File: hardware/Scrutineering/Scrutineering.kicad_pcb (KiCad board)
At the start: 2 copper layers, 52.8 x 51.7 mm, 22 parts, among them J1 Conn_02x04, J10 Conn_01x01, J11 Conn_01x02, J12 Conn_01x02, J2 Conn_02x04, J3 Conn_01x03, J4 Conn_01x03, J5 Conn_01x01, J6 Conn_01x01, J7 Conn_01x01, J8 Conn_01x01, J9 Conn_01x01

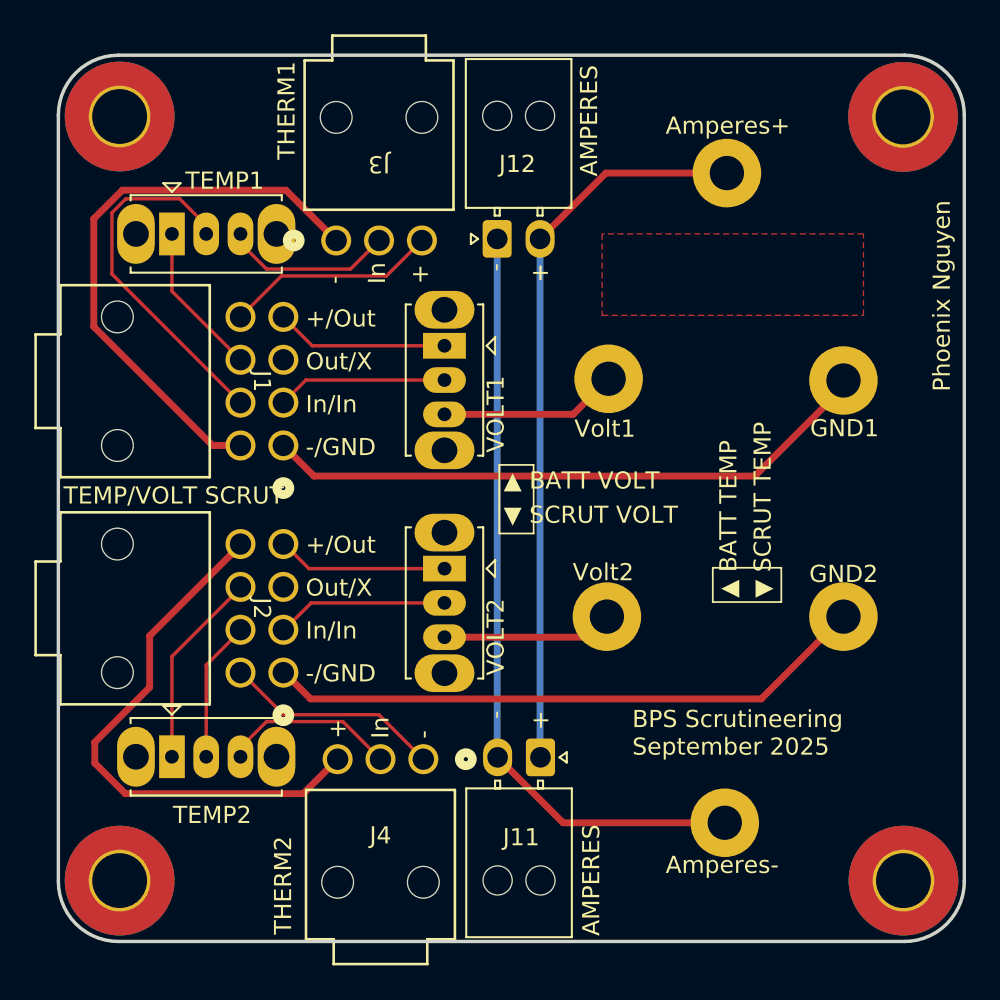
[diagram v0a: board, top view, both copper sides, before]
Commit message: changed to vertical connectors
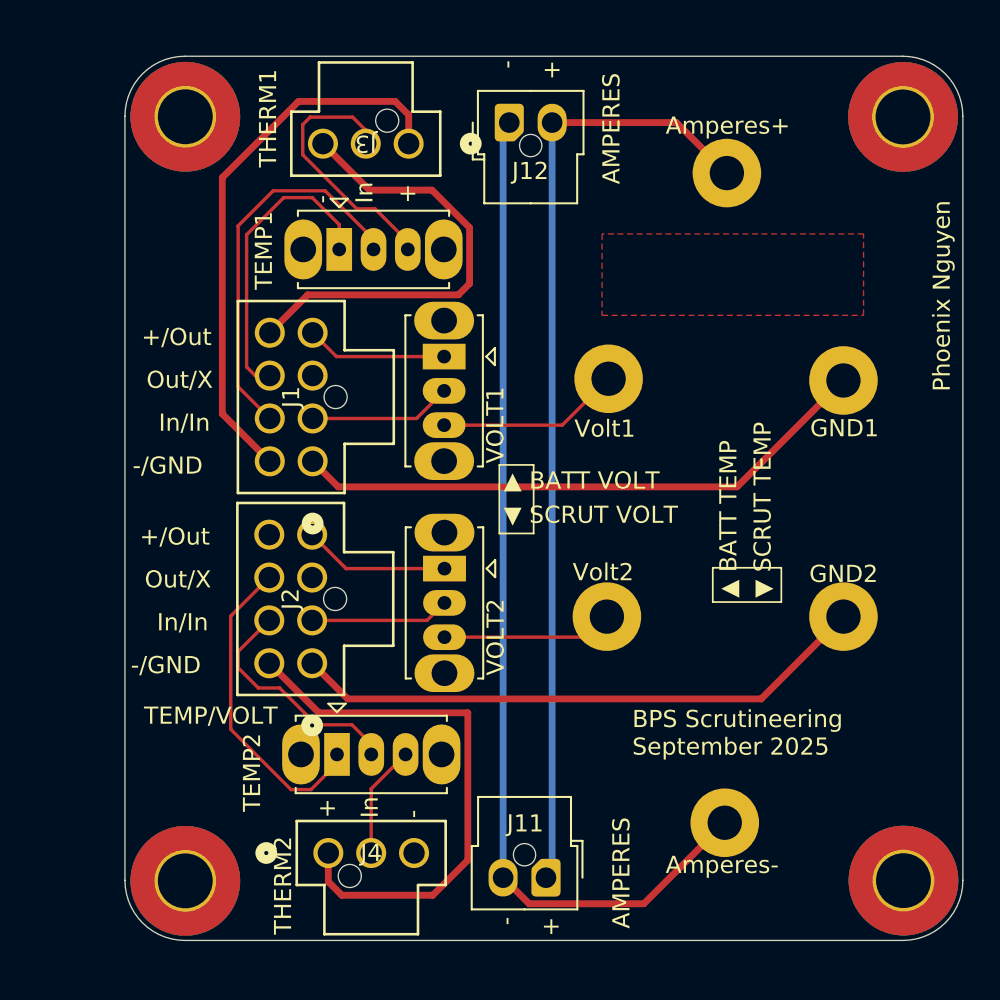
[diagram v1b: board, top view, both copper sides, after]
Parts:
- J1, J2: footprint Scrutineering:nanofit_02x04 -> Scrutineering:CONN_SD-105310-100_08_MOL
- J11, J12: footprint UTSVT_Connectors:105313-2102 -> UTSVT_Connectors:Molex_Nano-Fit_105309-xx02_1x02_P2.50mm_Vertical
- J3, J4: footprint VoltTemp:1053131103 -> Scrutineering:CONN_SD-105309-100_03_MOL
- moved TEMP1 9.80 mm to (103.8, 63.8)
- moved TEMP2 9.63 mm to (103.6, 93.2)
- moved J4 7.79 mm to (103.1, 99.0)
- moved J3 7.05 mm to (107.8, 57.6)
- moved J11 7.03 mm to (115.8, 100.4)
- moved J12 6.82 mm to (113.7, 56.4)
- moved MH3 3.83 mm to (94.8, 56.0)
- moved MH4 3.83 mm to (94.8, 100.6)
- moved J1 1.94 mm to (102.2, 76.1), turned to 90 degrees
- moved J2 1.77 mm to (102.2, 87.9), turned to 90 degrees
- moved VOLT1 0.63 mm to (109.9, 70.0)
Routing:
- net /VDDA_8: track 32.9 -> 0.00 mm
- net /GNDA_8: track 12.8 -> 32.4 mm
- net /scrut-: track 45.1 -> 59.7 mm
- net /VDDA_7: track 12.4 -> 26.8 mm
- net /scrut+: track 42.7 -> 55.6 mm
- net /rawTemp7: track 9.00 -> 17.7 mm
- net /rawTemp8: track 12.1 -> 18.6 mm
- net /scrutTemp7: track 9.94 -> 15.4 mm
- net /inputTemp8: track 8.92 -> 13.8 mm
- net /scrutTemp8: track 10.2 -> 6.58 mm
- net /inputVolt8: track 10.0 -> 8.14 mm
- net /voltTap7: track 10.1 -> 8.25 mm
- net /inputVolt7: track 9.95 -> 8.34 mm
- net /voltTap8: track 9.99 -> 8.54 mm
- net /GND_Seg8: track 35.3 -> 33.8 mm
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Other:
- board size 52.8 x 51.7 mm -> 48.9 x 51.6 mm
- board text added: "TEMP/VOLT"
- board text removed: "TEMP/VOLT SCRUT"
